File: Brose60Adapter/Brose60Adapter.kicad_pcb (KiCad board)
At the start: 2 copper layers, 80 x 66 mm, 6 parts, among them CN1 Conn_02x30_Odd_Even, CN2 FP2800A, CN3 FP2800A

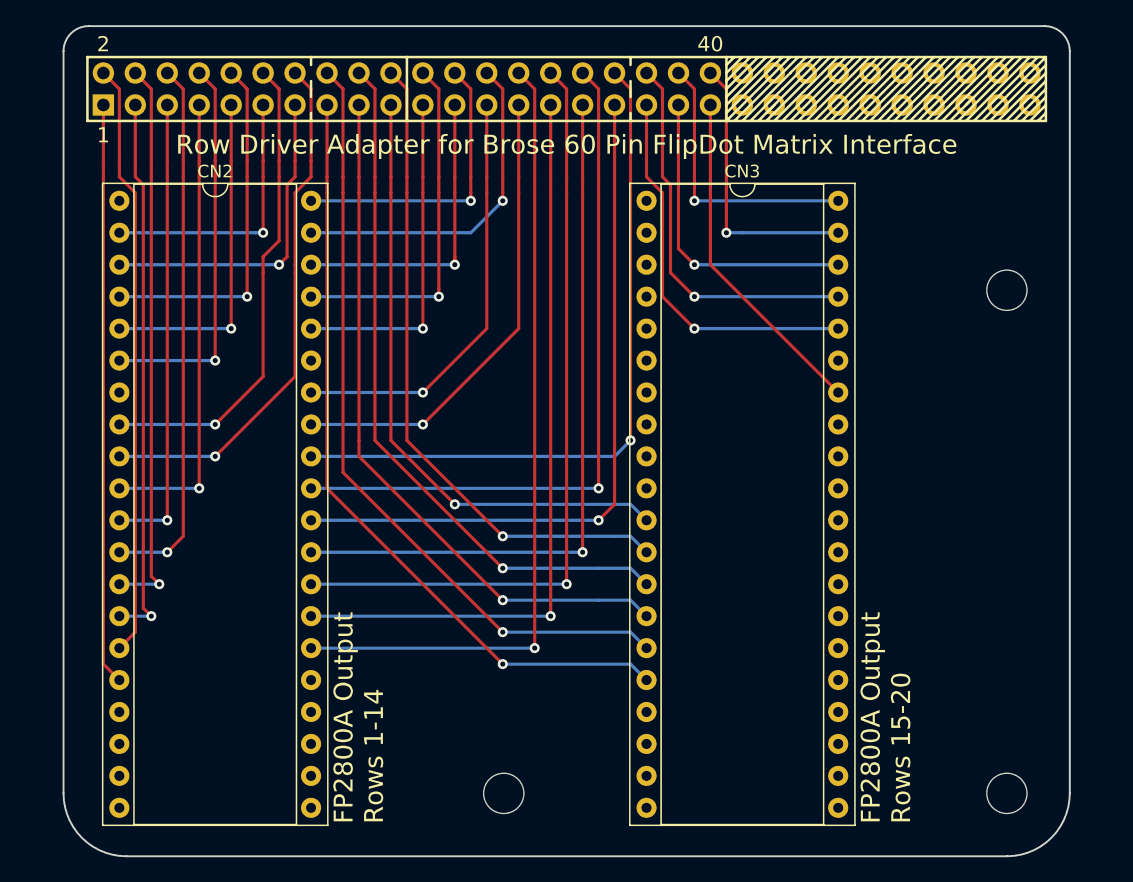
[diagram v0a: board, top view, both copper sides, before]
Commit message: - Using DIP32 instead of DIP40 for FP2800A-Outputs - Shrinking Board to 80x55, re-aligning mounting holes to be in 5 mm raster - Labeling sheet and pcb plan - adding text and drawing on pcb
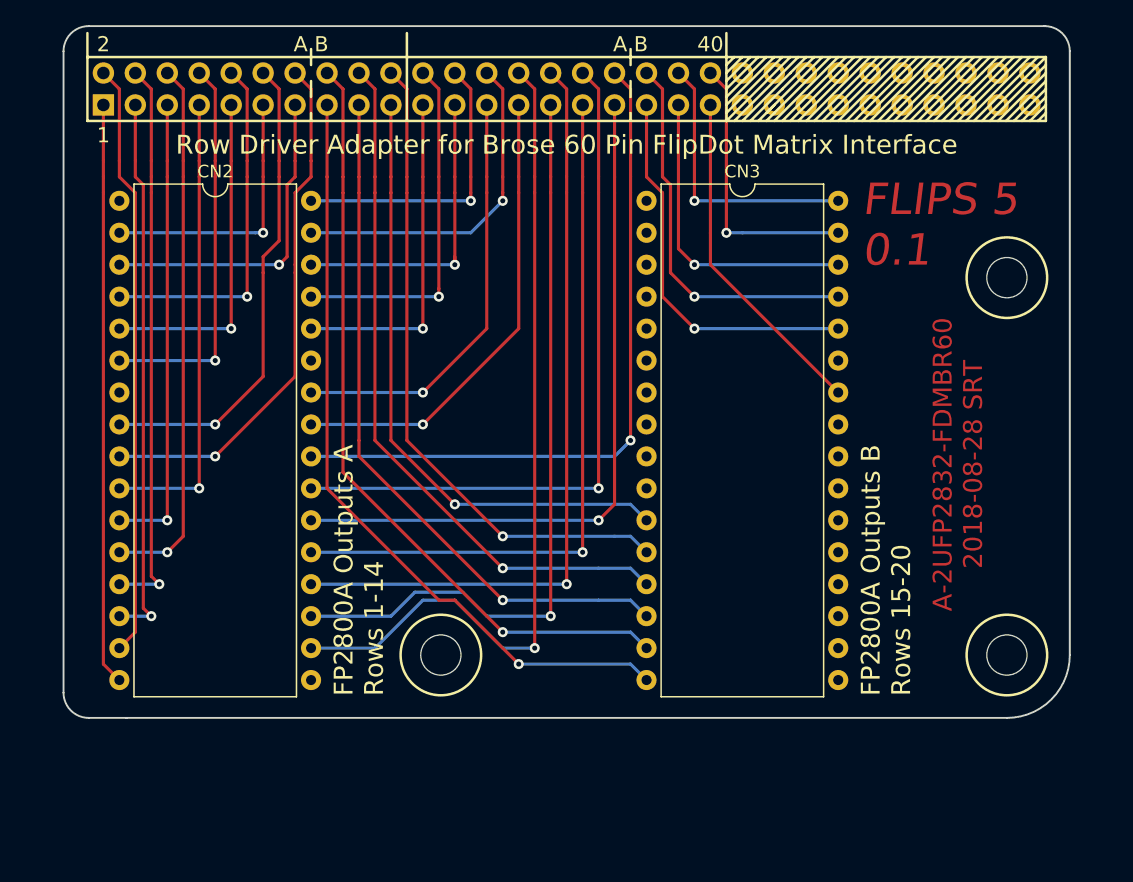
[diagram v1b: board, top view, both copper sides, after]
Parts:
- CN2, CN3: footprint Housings_DIP:DIP-40_W15.24mm_Socket -> Own:DIP-32-from-40_W15.24mm
- moved REF** 12.1 mm to (98.0, 127.5)
- moved REF** 11.0 mm to (142.9, 127.5)
- moved REF** 1.00 mm to (142.9, 97.5)
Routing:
- net Net-(CN1-Pad28): track 64.0 -> 67.2 mm
- net Net-(CN1-Pad29): track 59.7 -> 61.3 mm
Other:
- board size 80 x 66 mm -> 80 x 55 mm
- board text added: "A B"
- board text added: "A-2UFP2832-FDMBR60 2018-08-28 SRT"
- board text added: "FLIPS 5 0.1"
- board text added: "FP2800A Outputs A Rows 1-14"
- board text added: "FP2800A Outputs B Rows 15-20"
- board text removed: "FP2800A Output Rows 1-14"
- board text removed: "FP2800A Output Rows 15-20"
